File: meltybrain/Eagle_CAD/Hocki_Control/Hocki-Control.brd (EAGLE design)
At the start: 90 x 46 mm, 148 parts, among them CN1 JST_2PIN, J1 SM03B-SRSS-TB(LF)(SN), J2 SM04B-SRSS-TB(LF)(SN), J3 SM04B-SRSS-TB(LF)(SN), J4 SM04B-SRSS-TB(LF)(SN), J5 SM03B-SRSS-TB(LF)(SN), J6 SM03B-SRSS-TB(LF)(SN), U1 AP63200, U10 LMH6612MAX/NOPB, U11 TLV3502AIDCNR, U12 LMH6612MAX/NOPB, U13 TMP235A4DCKR, U14 ADXL375, U15 NL27WZ32USG, U16 ADXL375, U17 ADXL375, U18 NL27WZ32USG, U19 ADXL375, U2 TEENSY_4.1, U20 AD8426ACPZ-WP, U21 LMH6612MAX/NOPB, U22 HMC1052L-TR, U23 LMH6612MAX/NOPB, U24 IRF7509, U3 AP2210K-5.0TRG1, U4 AP2210K-3.3TRG1, U5 HEF4104BT,653, U6 LDL212PU50R, U7 LMH6612MAX/NOPB, U8 LMH6612MAX/NOPB, U9 TMUX1219DCKR

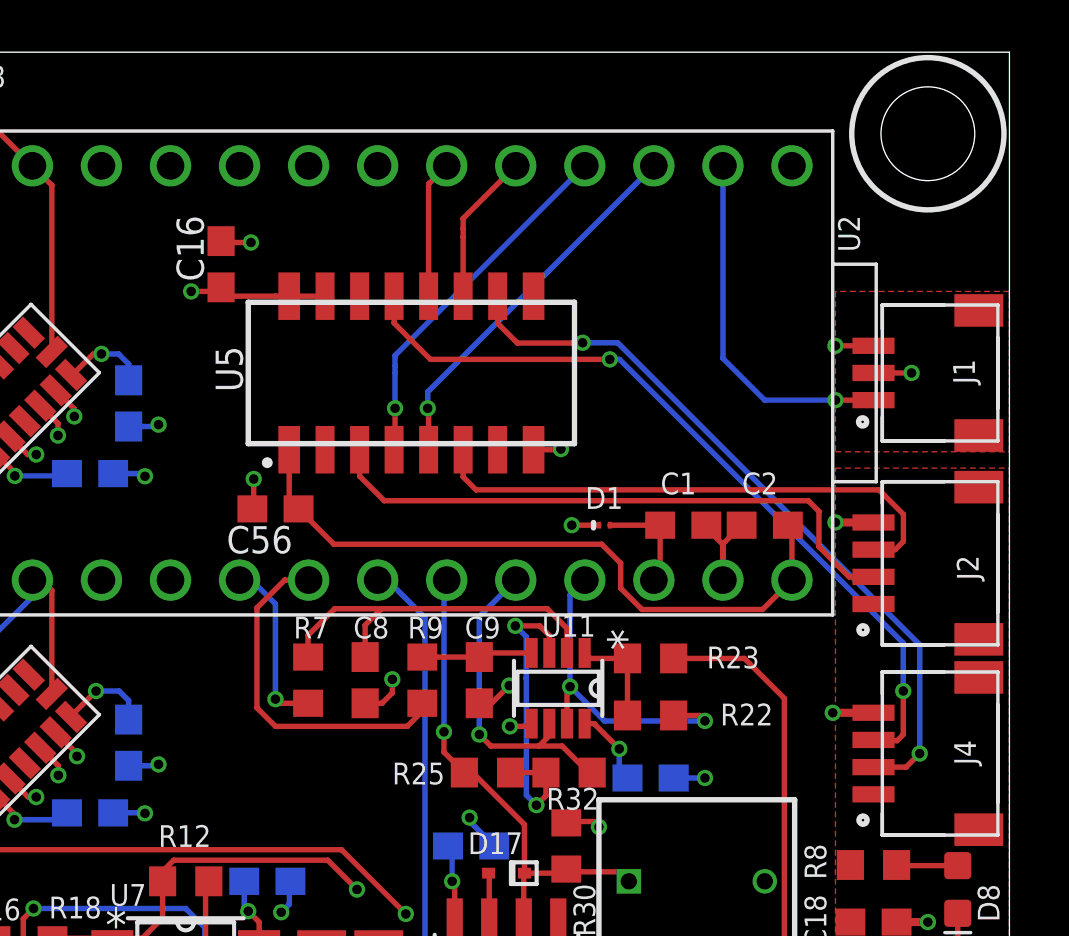
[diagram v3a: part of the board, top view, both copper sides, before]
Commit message: Replaced levels shifter with TXB0106 and level-shifted radio signal
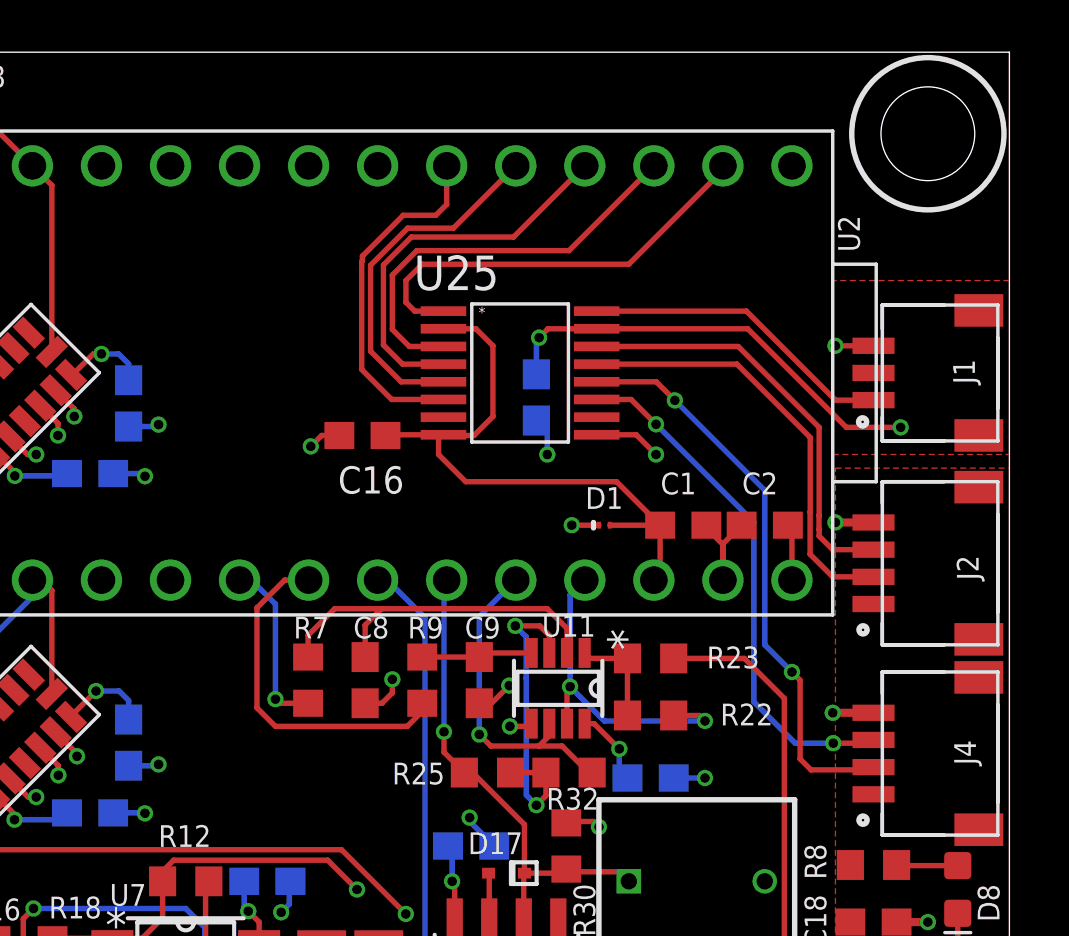
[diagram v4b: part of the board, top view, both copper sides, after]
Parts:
- removed U5: HEF4104BT,653, Hocki_Library:16-SOIC
- added U25: TXB0106PWR, RoboJackets-ICs:PW16
- moved C56 10.4 mm to (20.6, 6.10), flipped to the bottom, turned to 270 degrees
- moved C16 8.17 mm to (14.2, 4.70), turned to 180 degrees
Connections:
- new net A_RC_SIGNAL: U2.0, U25.1
- net 3.3V: now also U25.2, U25.8; no longer J1.2, J1.S1, J1.S2, U5.15, U5.16
- net 5V: now also J1.2, J1.S1, J1.S2, U25.15; no longer U5.1
- net B_LED_CLK1: now also U25.13; no longer U5.3
- net B_LED_CLK2: now also U25.12; no longer U5.10
- net B_LED_DATA1: now also U25.14; no longer U5.6
- net B_LED_DATA2: now also U25.11; no longer U5.13
- net GND: now also U25.9; no longer U5.8
- net LED_CLK1: now also U25.4; no longer U5.4
- net LED_CLK2: now also U25.5; no longer U5.11
- net LED_DATA1: now also U25.3; no longer U5.5
- net LED_DATA2: now also U25.6; no longer U5.12
- net RC_SIGNAL: now also U25.16; no longer U2.0
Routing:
- net A_RC_SIGNAL: track 0.00 -> 15.8 mm
- net B_LED_DATA2: track 29.2 -> 19.3 mm
- net LED_DATA2: track 5.07 -> 13.0 mm
- net LED_CLK2: track 5.60 -> 13.2 mm
- net B_LED_CLK1: track 22.2 -> 15.9 mm
- net B_LED_CLK2: track 27.3 -> 21.2 mm
- net B_LED_DATA1: track 20.0 -> 15.6 mm
- net 3.3V: track 69.4 -> 65.3 mm, vias 16 -> 14
- net GND: track 123.7 -> 125.6 mm
- net RC_SIGNAL: track 13.3 -> 11.5 mm, vias 1 -> 0
- net LED_DATA1: track 13.9 -> 15.4 mm, vias 1 -> 0
- net LED_CLK1: track 13.4 -> 14.4 mm, vias 1 -> 0
- net 5V: track 53.6 -> 54.3 mm, vias 9 -> 11
- added copper zone on layer 1, net 5V
- removed copper zone on layer 1, net 3.3V

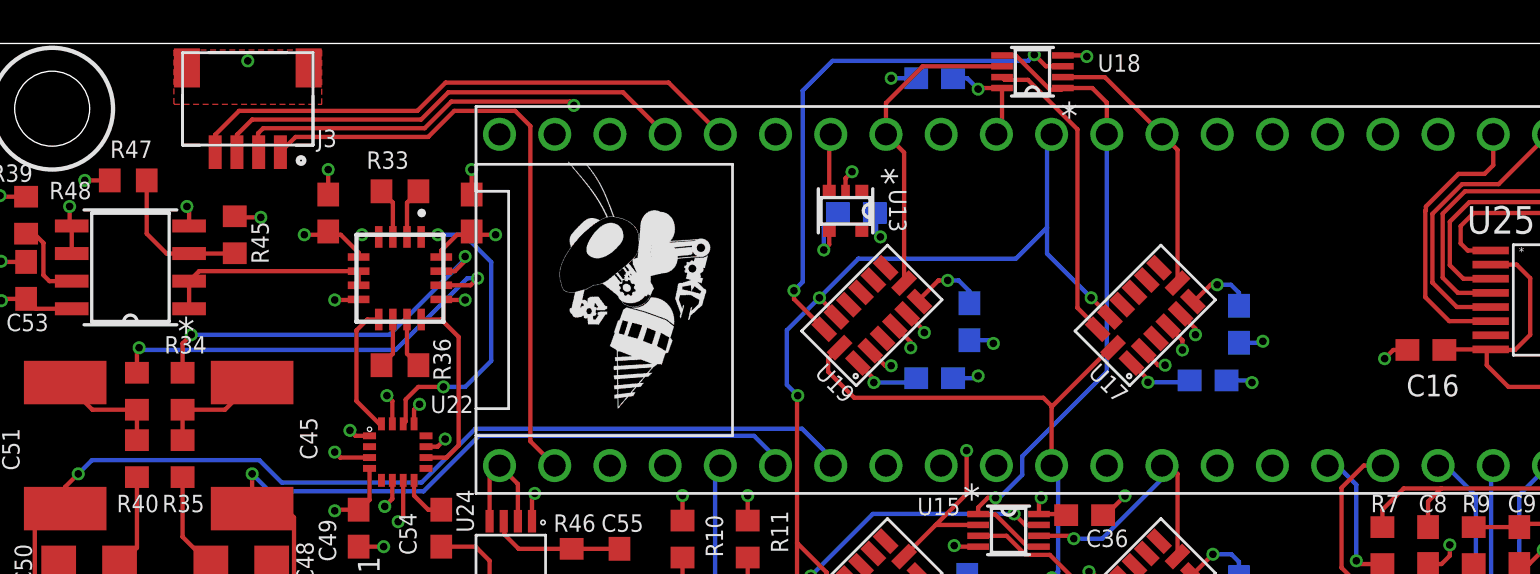
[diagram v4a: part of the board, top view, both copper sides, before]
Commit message: Split 4-pin ESC connector into 2x 2-pin connectors
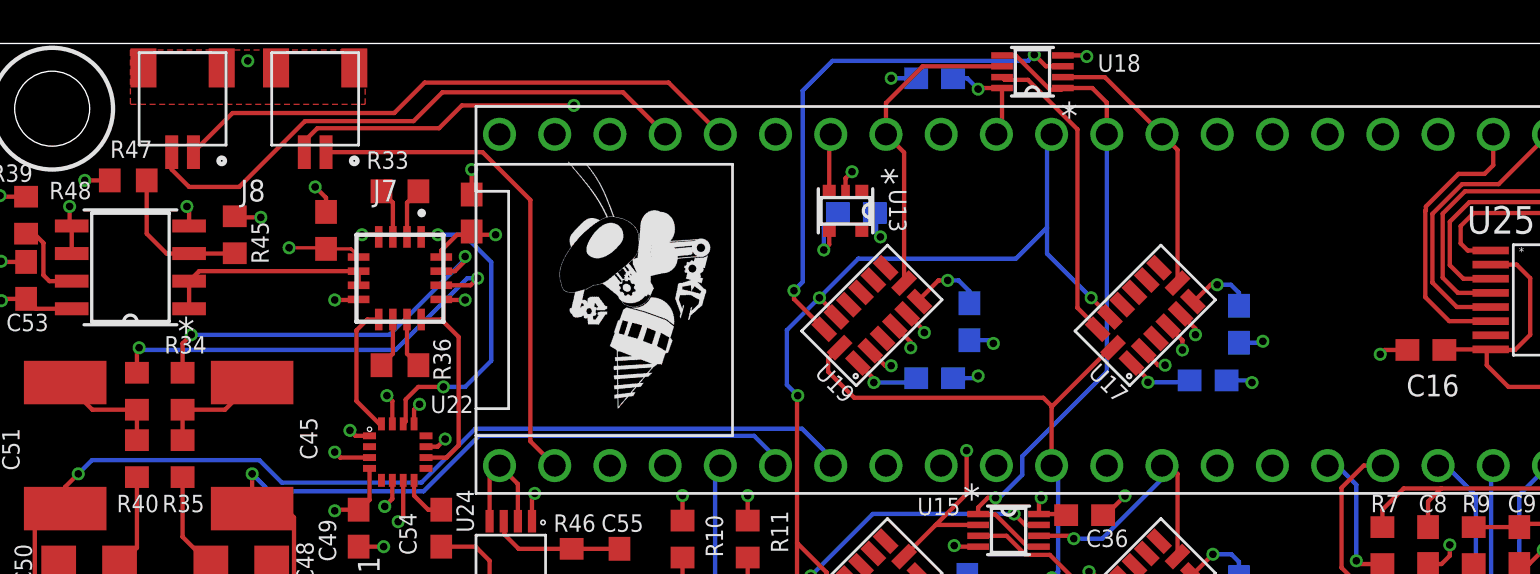
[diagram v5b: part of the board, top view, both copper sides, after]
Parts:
- removed J3: SM04B-SRSS-TB(LF)(SN), Hocki_Library:SM04B-SRSS-TB(LF)(SN)
- added J7, J8: SM02B-SRSS-TB(LF)(SN), Hocki_Library:SM02B-SRSS-TB(LF)(SN)
- moved C44 0.81 mm to (-36.4, 10.2)
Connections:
- net ESC_L: now also J8.2; no longer J3.3
- net ESC_R: now also J7.2; no longer J3.2
- net ESC_TEL_L: now also J8.1; no longer J3.4
- net ESC_TEL_R: now also J7.1; no longer J3.1
- net GND: now also J7.S1, J7.S2, J8.S1, J8.S2; no longer J3.S1, J3.S2
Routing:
- net ESC_TEL_R: track 28.7 -> 23.0 mm
- net ESC_L: track 22.1 -> 26.4 mm
- net ESC_R: track 33.5 -> 31.0 mm
- net ESC_TEL_L: track 26.0 -> 26.6 mm
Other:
- board text added: "Hocki Control V2"
- board text removed: "Hocki Control V1"

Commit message: tweaks
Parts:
- moved J8 1.00 mm to (-42.0, 13.8)
- moved C16 0.94 mm to (14.7, 3.90), turned to 270 degrees
- moved J7 0.90 mm to (-36.0, 13.8)
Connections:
- net ESC_L: now also J8.1; no longer J8.2
- net ESC_TEL_L: now also J8.2; no longer J8.1
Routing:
- net 3.3V: track 65.3 -> 56.1 mm, vias 14 -> 15
- net ESC_L: track 26.4 -> 23.2 mm
- net 5V: track 54.3 -> 52.2 mm
- net LED_DATA2: track 13.0 -> 10.9 mm
- net GND: track 125.9 -> 124.5 mm
- net ESC_TEL_R: track 23.0 -> 23.7 mm
- net LED_CLK2: track 13.2 -> 12.7 mm

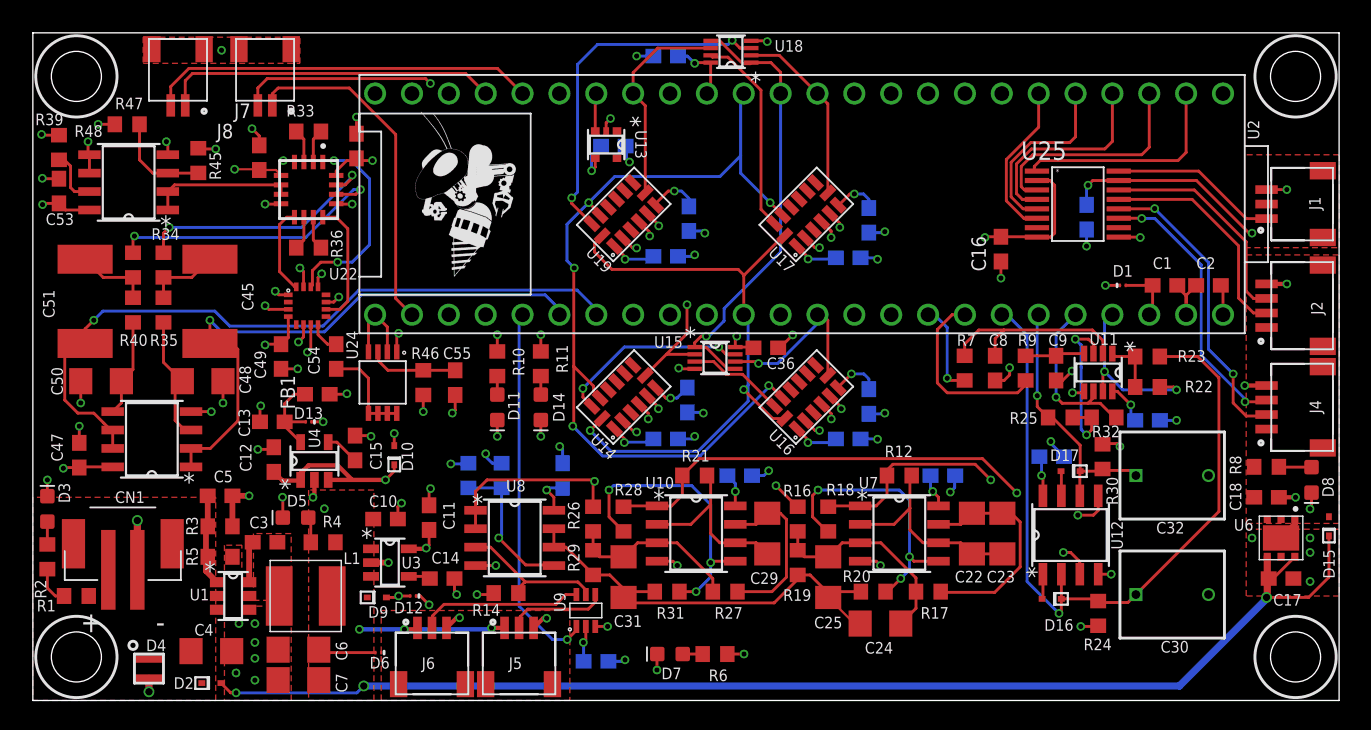
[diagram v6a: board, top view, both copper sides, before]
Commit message: Accelerometer rotation + silkscreen
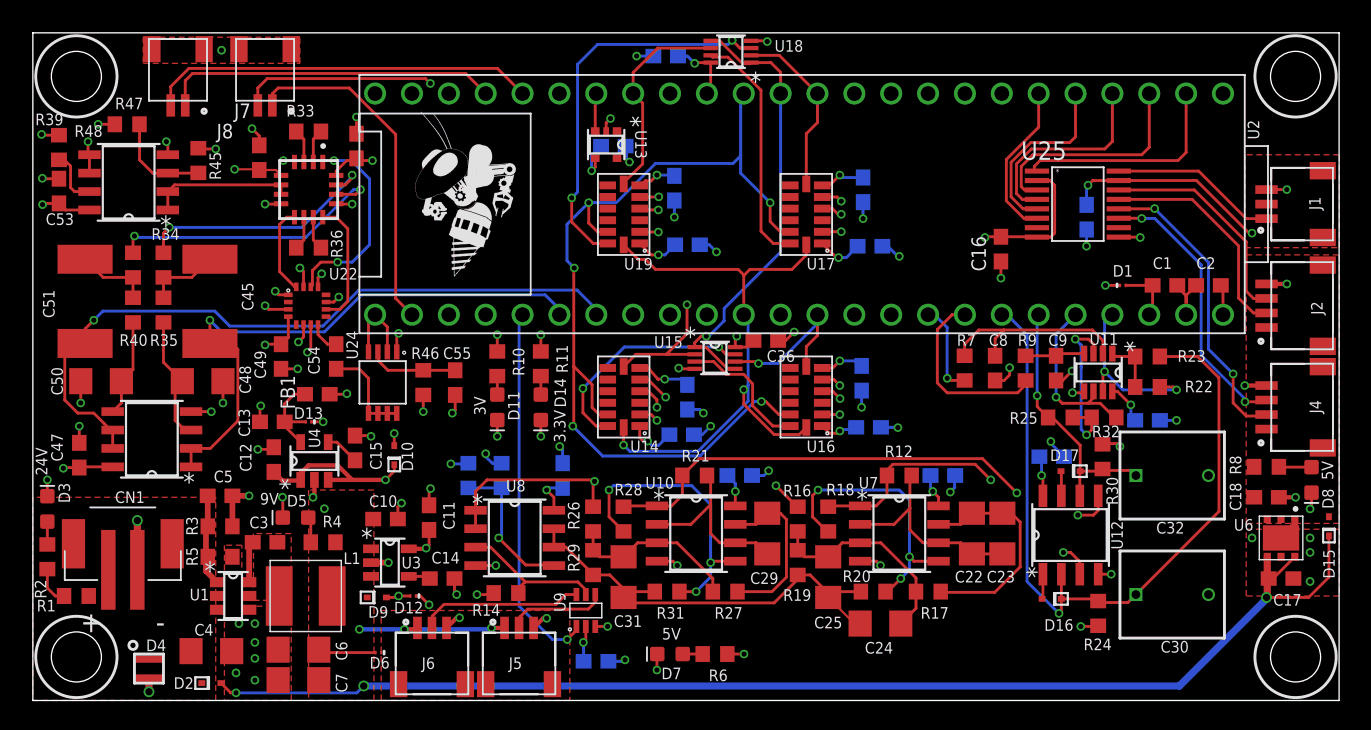
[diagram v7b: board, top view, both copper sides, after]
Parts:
- moved C43 2.33 mm to (-7.80, 8.10)
- moved C41 2.14 mm to (5.20, 7.98)
- moved C42 1.70 mm to (-6.90, 4.20)
- moved C40 1.70 mm to (5.68, 4.10)
- moved C38 1.68 mm to (5.10, -5.00)
- moved C37 1.61 mm to (5.58, -8.38)
- moved C34 1.14 mm to (-7.30, -8.88)
- moved C36 0.50 mm to (-1.50, -2.40)
- moved C35 0.20 mm to (-6.90, -6.30)
- turned U14 to 180 degrees
- turned U16 to 180 degrees
- turned U17 to 180 degrees
- turned U19 to 180 degrees
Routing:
- net MISO: track 59.6 -> 64.8 mm
- net GND: track 124.5 -> 127.8 mm
- net MOSI2: track 6.77 -> 9.33 mm
- net MOSI3: track 14.0 -> 16.5 mm
- net MOSI4: track 24.6 -> 27.0 mm
- net MOSI1: track 13.4 -> 15.7 mm
- net SCLK: track 43.2 -> 41.7 mm
- net CS1: track 15.0 -> 16.3 mm
- net CS2: track 12.1 -> 11.4 mm
- net 3.3V: track 56.1 -> 55.4 mm
- net CS3: track 12.8 -> 12.2 mm
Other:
- board text added: "24V"
- board text added: "3.3V"
- board text added: "3V"
- board text added: "5V"
- board text added: "9V"

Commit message: CTRL BRD improvements
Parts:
- moved C34 3.77 mm to (-11.0, -8.18), turned to 0 degrees
- moved C35 1.00 mm to (-7.90, -6.30)
- moved C43 0.41 mm to (-7.90, 7.70)
- moved C38 0.40 mm to (4.70, -5.00)
- moved C40 0.36 mm to (5.48, 3.80)
- moved C36 0.32 mm to (-1.60, -2.10), flipped to the bottom, turned to 180 degrees
- moved C42 0.10 mm to (-7.00, 4.20)
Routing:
- net MISO: track 64.8 -> 61.1 mm
- net GND: track 127.8 -> 124.8 mm
- net 3.3V: track 55.4 -> 52.5 mm
- net CS2: track 11.4 -> 9.29 mm, vias 1 -> 0
- net CS1: track 16.3 -> 14.3 mm, vias 1 -> 0
- net SCLK: track 41.7 -> 40.1 mm
- net MOSI2: track 9.33 -> 8.43 mm
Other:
- board text added: "3V3"
- board text removed: "3V"
